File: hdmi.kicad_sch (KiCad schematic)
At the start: 10 parts, among them J6 HDMI_A, U4 AP22615AWU

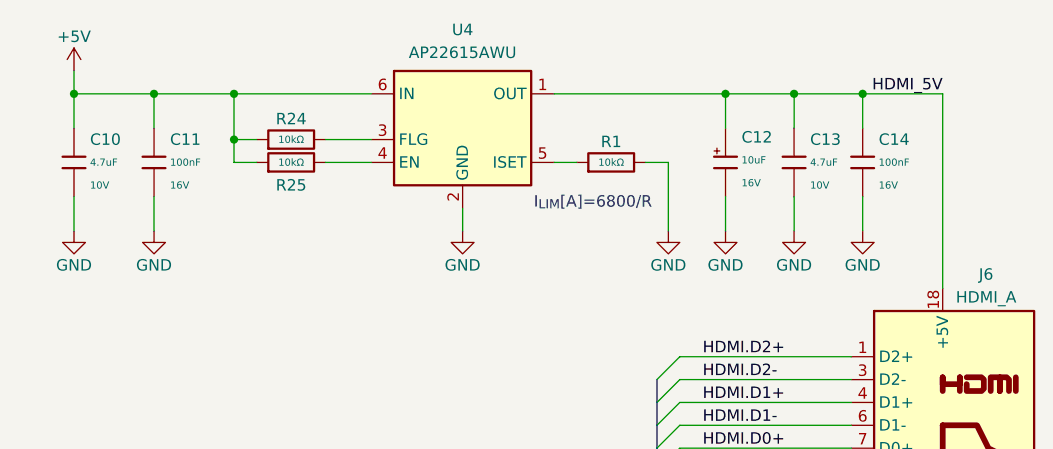
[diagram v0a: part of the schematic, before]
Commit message: [#1] WIP: Change components to ones from the global library, refactor schematic
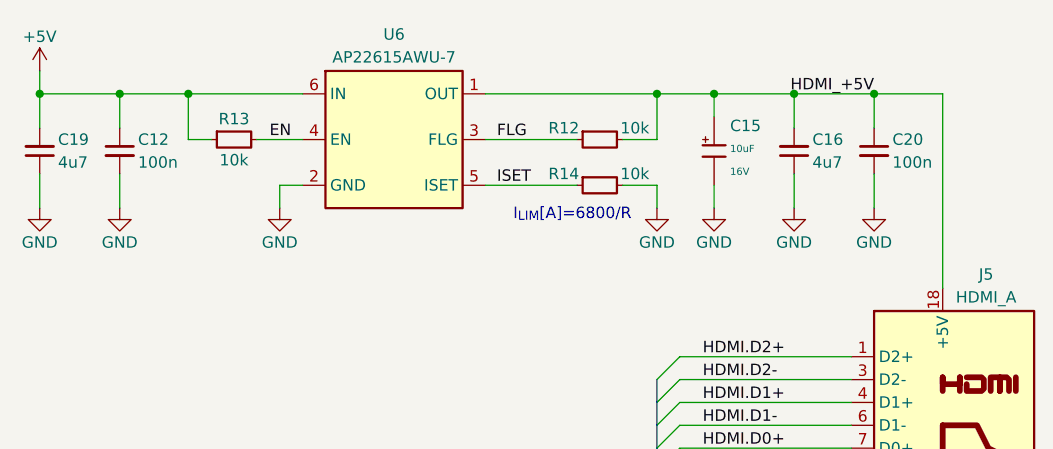
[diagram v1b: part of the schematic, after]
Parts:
- removed C10, C13: 4.7uF, PCM_JLCPCB:C_0402, symbol PCM_JLCPCB-Capacitors:0402,4.7uF
- removed C11, C14: 100nF, PCM_JLCPCB:C_0402, symbol PCM_JLCPCB-Capacitors:0402,100nF
- removed C12: 10uF, PCM_JLCPCB:C_CASE-A-3216-18(mm), symbol PCM_JLCPCB-Capacitors:CASE-A-3216-18(mm),10uF
- removed R1, R24, R25: 10kΩ, PCM_JLCPCB:R_0402, symbol PCM_JLCPCB-Resistors:0402,10kΩ
- removed U4: AP22615AWU, Package_TO_SOT_SMD:SOT-23-6, symbol Regulator_Linear:AP22615AWU
- added C12, C20: C-100n-0402, DW-footprints:C_0402_1005Metric, symbol DW-capacitors:C-100n-0402
- added C15: 10uF, PCM_JLCPCB:C_CASE-A-3216-18(mm), symbol PCM_JLCPCB-Capacitors:CASE-A-3216-18(mm),10uF
- added C16, C19: C-4u7-0402, DW-footprints:C_0402_1005Metric, symbol DW-capacitors:C-4u7-0402
- added R12, R13, R14: R-10k-0402, DW-footprints:R_0402_1005Metric, symbol DW-resistors:R-10k-0402
- added U6: AP22615AWU-7, DW-footprints:TSOT-23-6, symbol DW-ICs:AP22615AWU-7
- renumbered J6 to J5
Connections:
- net +5V: now also C12.1, C19.2, R13.1, U6.6 (IN)
- net GND: now also C12.2, C15.2, C16.1, C19.1, C20.2, R14.2, U6.2 (GND)
- net HDMI_5V renamed HDMI_+5V
- net HDMI_+5V: now also C15.1, C16.2, C20.1, R12.2, U6.1 (OUT)
- new net EN: R13.2, U6.4 (EN)
- new net FLG: R12.1, U6.3 (FLG)
- new net ISET: R14.1, U6.5 (ISET)

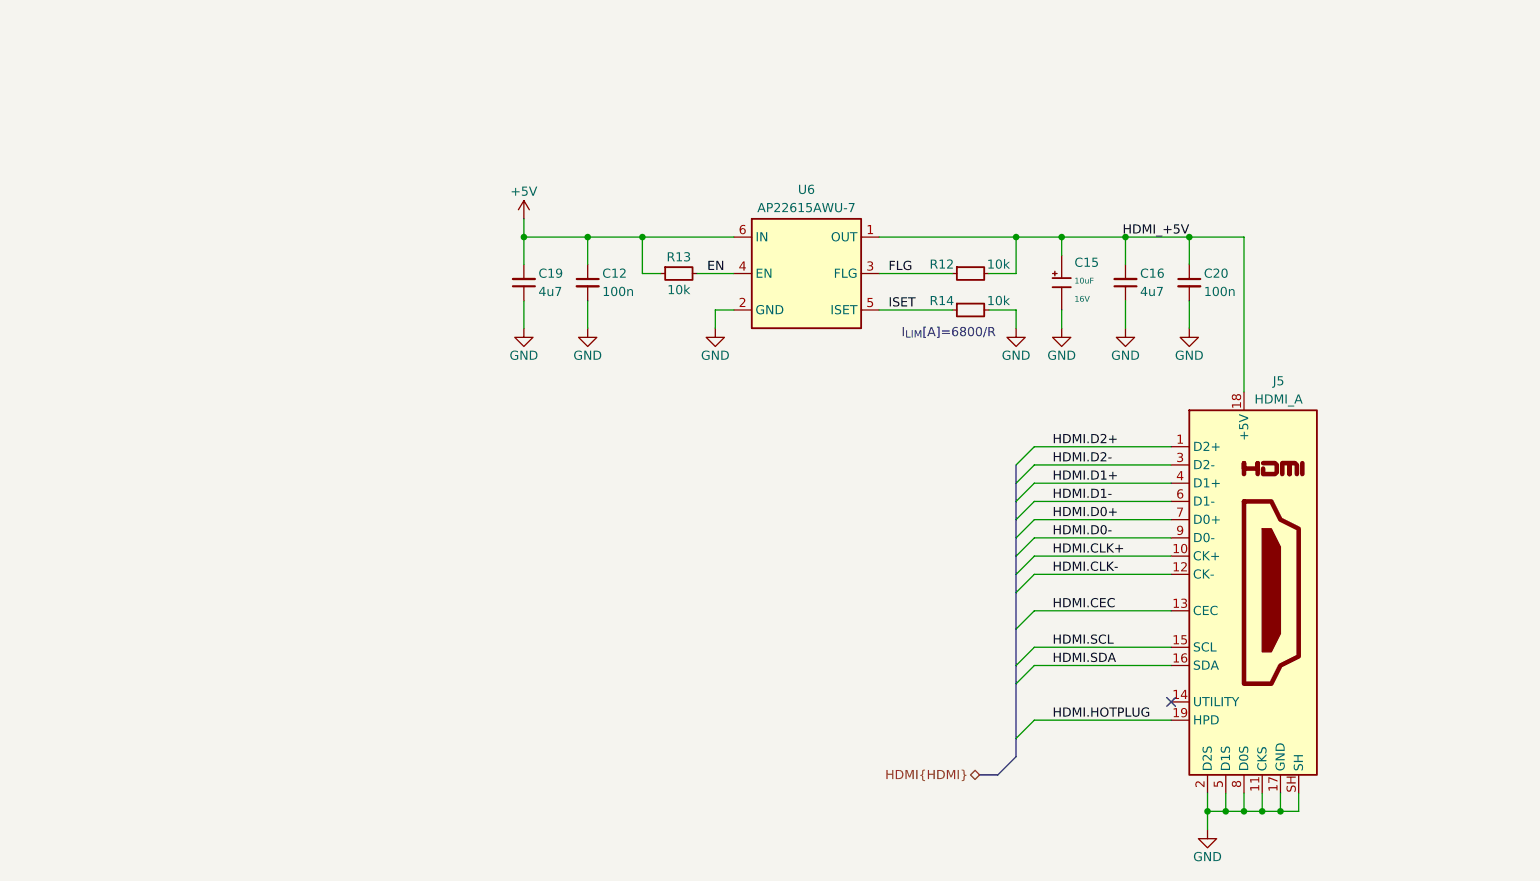
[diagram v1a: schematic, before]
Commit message: [#1] Change components to ones from the global library, add debug console, refactor schematic
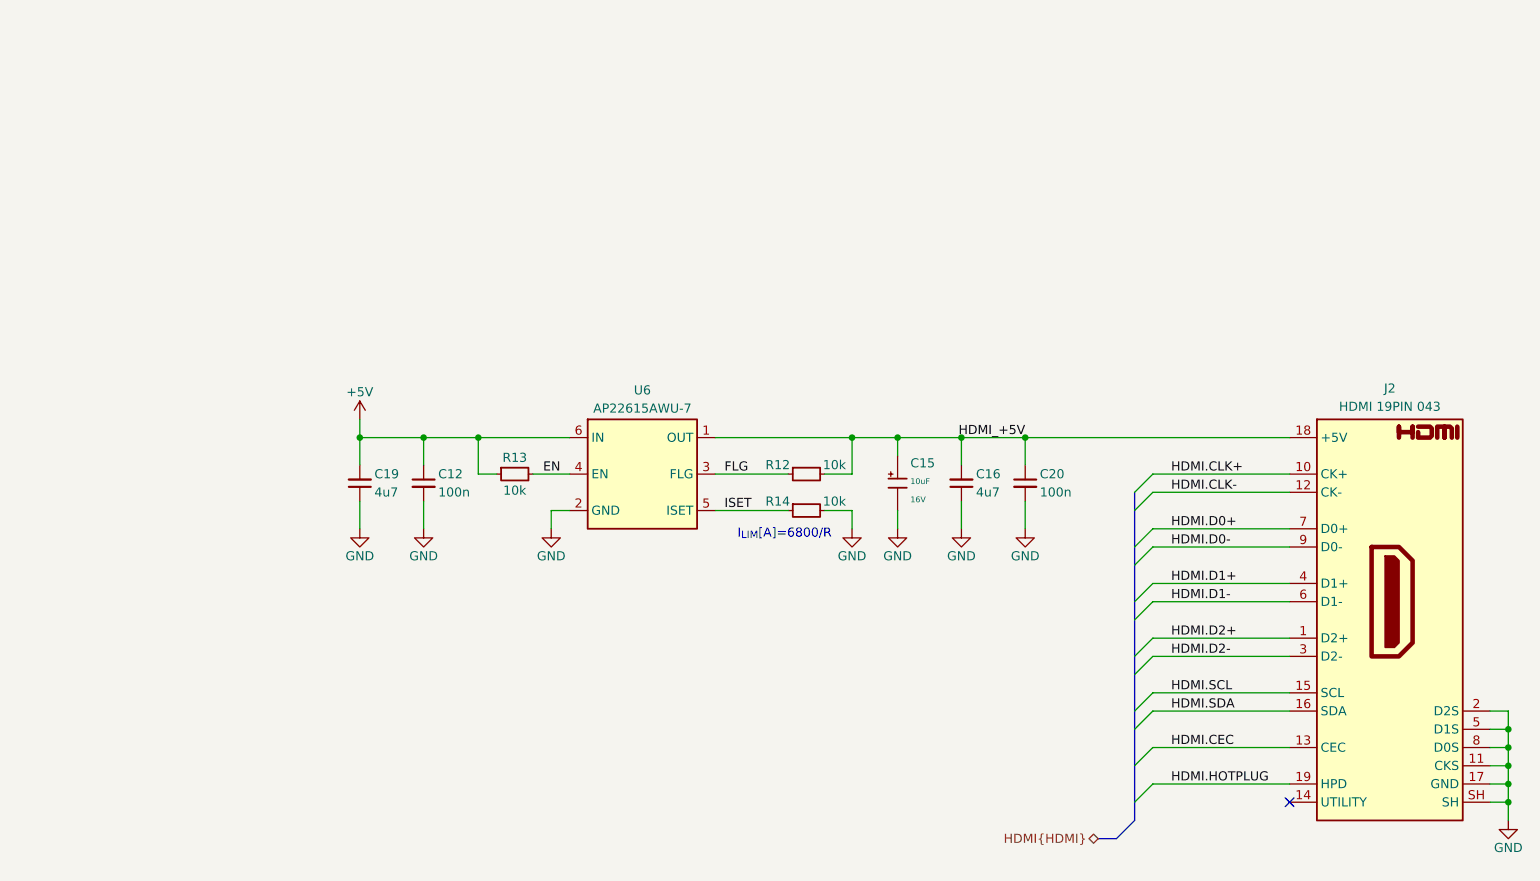
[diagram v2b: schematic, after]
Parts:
- removed J5: HDMI_A, Connector_Video:HDMI_A_Molex_208658-1001_Horizontal, symbol Connector:HDMI_A
- added J2: HDMI-A_HDMI-19PIN-043, DW-footprints:Conn_HDMI-A_HDMI-19PIN-043, symbol DW-connectors:HDMI-A_HDMI-19PIN-043
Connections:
- net GND: now also J2.11 (CKS), J2.17 (GND), J2.2 (D2S), J2.5 (D1S), J2.8 (D0S), J2.SH
- net HDMI.CEC: now also J2.13 (CEC)
- net HDMI.CLK+: now also J2.10 (CK+)
- net HDMI.CLK-: now also J2.12 (CK-)
- net HDMI.D0+: now also J2.7 (D0+)
- net HDMI.D0-: now also J2.9 (D0-)
- net HDMI.D1+: now also J2.4 (D1+)
- net HDMI.D1-: now also J2.6 (D1-)
- net HDMI.D2+: now also J2.1 (D2+)
- net HDMI.D2-: now also J2.3 (D2-)
- net HDMI.HOTPLUG: now also J2.19 (HPD)
- net HDMI.SCL: now also J2.15 (SCL)
- net HDMI.SDA: now also J2.16 (SDA)
- net HDMI_+5V: now also J2.18 (+5V)
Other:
- moved on the sheet: C12, C15, C16, C19, C20, R12, R13, R14, U6

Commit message: [#1] Re-annotate schematic
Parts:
- renumbered C15 to C10, C19 to C11, C16 to C12, C12 to C8, C20 to C9, J2 to J8, R12 to R14, R14 to R15, U6 to U2
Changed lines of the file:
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@@
 		(on_board yes)
 		(dnp no)
-		(property "Reference" "R12"
+		(property "Reference" "R14"
 			(at 172.974 134.62 0)
 			(effects
@@
 			(project "cm5-module"
 				(path "/090a8e41-87a8-4fb1-998b-60a2c0dc4cee/ad3d5826-cab5-4231-8219-c7d7eaea11f6"
-					(reference "R12")
+					(reference "R14")
 					(unit 1)
 				)
@@
 		(on_board yes)
 		(dnp no)
-		(property "Reference" "#PWR54"
+		(property "Reference" "#PWR048"
 			(at 187.96 149.86 0)
 			(effects
@@
 			(project "cm5-module"
 				(path "/090a8e41-87a8-4fb1-998b-60a2c0dc4cee/ad3d5826-cab5-4231-8219-c7d7eaea11f6"
-					(reference "#PWR54")
+					(reference "#PWR048")
 					(unit 1)
 				)
@@
 		(on_board yes)
 		(dnp no)
-		(property "Reference" "C20"
+		(property "Reference" "C9"
 			(at 207.772 135.89 90)
 			(effects
@@
 			(project "cm5-module"
 				(path "/090a8e41-87a8-4fb1-998b-60a2c0dc4cee/ad3d5826-cab5-4231-8219-c7d7eaea11f6"
-					(reference "C20")
+					(reference "C9")
 					(unit 1)
 				)
@@
 		(on_board yes)
 		(dnp no)
-		(property "Reference" "#PWR55"
+		(property "Reference" "#PWR049"
 			(at 196.85 149.86 0)
 			(effects
@@
 			(project "cm5-module"
 				(path "/090a8e41-87a8-4fb1-998b-60a2c0dc4cee/ad3d5826-cab5-4231-8219-c7d7eaea11f6"
-					(reference "#PWR55")
+					(reference "#PWR049")
 					(unit 1)
 				)
@@
 		(on_board yes)
 		(dnp no)
-		(property "Reference" "#PWR39"
+		(property "Reference" "#PWR045"
 			(at 121.92 149.86 0)
 			(effects
@@
 			(project "cm5-module"
 				(path "/090a8e41-87a8-4fb1-998b-60a2c0dc4cee/ad3d5826-cab5-4231-8219-c7d7eaea11f6"
-					(reference "#PWR39")
+					(reference "#PWR045")
 					(unit 1)
 				)
@@
 		(on_board yes)
 		(dnp no)
-		(property "Reference" "J2"
+		(property "Reference" "J8"
 			(at 256.54 123.952 0)
 			(effects
@@
 			(project ""
 				(path "/090a8e41-87a8-4fb1-998b-60a2c0dc4cee/ad3d5826-cab5-4231-8219-c7d7eaea11f6"
-					(reference "J2")
+					(reference "J8")
 					(unit 1)
 				)
@@
 		(on_board yes)
 		(dnp no)
-		(property "Reference" "C19"
+		(property "Reference" "C11"
 			(at 115.062 135.89 90)
 			(effects
@@
 			(project "cm5-module"
 				(path "/090a8e41-87a8-4fb1-998b-60a2c0dc4cee/ad3d5826-cab5-4231-8219-c7d7eaea11f6"
-					(reference "C19")
+					(reference "C11")
 					(unit 1)
 				)
@@
 		(on_board yes)
 		(dnp no)
-		(property "Reference" "#PWR56"
+		(property "Reference" "#PWR050"
 			(at 205.74 149.86 0)
 			(effects
@@
 			(project "cm5-module"
 				(path "/090a8e41-87a8-4fb1-998b-60a2c0dc4cee/ad3d5826-cab5-4231-8219-c7d7eaea11f6"
-					(reference "#PWR56")
+					(reference "#PWR050")
 					(unit 1)
 				)
@@
 		(on_board yes)
 		(dnp no)
-		(property "Reference" "#PWR40"
+		(property "Reference" "#PWR046"
 			(at 139.7 149.86 0)
 			(effects
@@
 			(project "cm5-module"
 				(path "/090a8e41-87a8-4fb1-998b-60a2c0dc4cee/ad3d5826-cab5-4231-8219-c7d7eaea11f6"
-					(reference "#PWR40")
+					(reference "#PWR046")
 					(unit 1)
 				)
@@
 		(on_board yes)
 		(dnp no)
-		(property "Reference" "C12"
+		(property "Reference" "C8"
 			(at 123.952 135.89 90)
 			(effects
@@
 			(project "cm5-module"
 				(path "/090a8e41-87a8-4fb1-998b-60a2c0dc4cee/ad3d5826-cab5-4231-8219-c7d7eaea11f6"
-					(reference "C12")
+					(reference "C8")
 					(unit 1)
 				)
@@
 		(on_board yes)
 		(dnp no)
-		(property "Reference" "U6"
+		(property "Reference" "U2"
 			(at 152.4 124.206 0)
 			(effects
@@
 			(project "cm5-module"
 				(path "/090a8e41-87a8-4fb1-998b-60a2c0dc4cee/ad3d5826-cab5-4231-8219-c7d7eaea11f6"
-					(reference "U6")
+					(reference "U2")
 					(unit 1)
 				)
@@
 		(on_board yes)
 		(dnp no)
-		(property "Reference" "#PWR35"
+		(property "Reference" "#PWR044"
 			(at 113.03 149.86 0)
 			(effects
@@
 			(project "cm5-module"
 				(path "/090a8e41-87a8-4fb1-998b-60a2c0dc4cee/ad3d5826-cab5-4231-8219-c7d7eaea11f6"
-					(reference "#PWR35")
+					(reference "#PWR044")
 					(unit 1)
 				)
@@
 		(on_board yes)
 		(dnp no)
-		(property "Reference" "C15"
+		(property "Reference" "C10"
 			(at 189.738 134.3659 0)
 			(effects
@@
 			(project "cm5-module"
 				(path "/090a8e41-87a8-4fb1-998b-60a2c0dc4cee/ad3d5826-cab5-4231-8219-c7d7eaea11f6"
-					(reference "C15")
+					(reference "C10")
 					(unit 1)
 				)
@@
 		(on_board yes)
 		(dnp no)
-		(property "Reference" "#PWR043"
+		(property "Reference" "#PWR051"
 			(at 273.05 190.5 0)
 			(effects
@@
 			(project "cm5-module"
 				(path "/090a8e41-87a8-4fb1-998b-60a2c0dc4cee/ad3d5826-cab5-4231-8219-c7d7eaea11f6"
-					(reference "#PWR043")
+					(reference "#PWR051")
 					(unit 1)
 				)
@@
 		(on_board yes)
 		(dnp no)
-		(property "Reference" "C16"
+		(property "Reference" "C12"
 			(at 198.882 135.89 90)
 			(effects
@@
 			(project "cm5-module"
 				(path "/090a8e41-87a8-4fb1-998b-60a2c0dc4cee/ad3d5826-cab5-4231-8219-c7d7eaea11f6"
-					(reference "C16")
+					(reference "C12")
 					(unit 1)
 				)
@@
 		(on_board yes)
 		(dnp no)
-		(property "Reference" "#PWR016"
+		(property "Reference" "#PWR043"
 			(at 113.03 132.08 0)
 			(effects
@@
 			(project "cm5-module"
 				(path "/090a8e41-87a8-4fb1-998b-60a2c0dc4cee/ad3d5826-cab5-4231-8219-c7d7eaea11f6"
-					(reference "#PWR016")
+					(reference "#PWR043")
 					(unit 1)
 				)
@@
 		(on_board yes)
 		(dnp no)
-		(property "Reference" "R14"
+		(property "Reference" "R15"
 			(at 172.974 139.7 0)
 			(effects
@@
 			(project "cm5-module"
 				(path "/090a8e41-87a8-4fb1-998b-60a2c0dc4cee/ad3d5826-cab5-4231-8219-c7d7eaea11f6"
-					(reference "R14")
+					(reference "R15")
 					(unit 1)
 				)
@@
 		(on_board yes)
 		(dnp no)
-		(property "Reference" "#PWR53"
+		(property "Reference" "#PWR047"
 			(at 181.61 149.86 0)
 			(effects
@@
 			(project "cm5-module"
 				(path "/090a8e41-87a8-4fb1-998b-60a2c0dc4cee/ad3d5826-cab5-4231-8219-c7d7eaea11f6"
-					(reference "#PWR53")
+					(reference "#PWR047")
 					(unit 1)
 				)

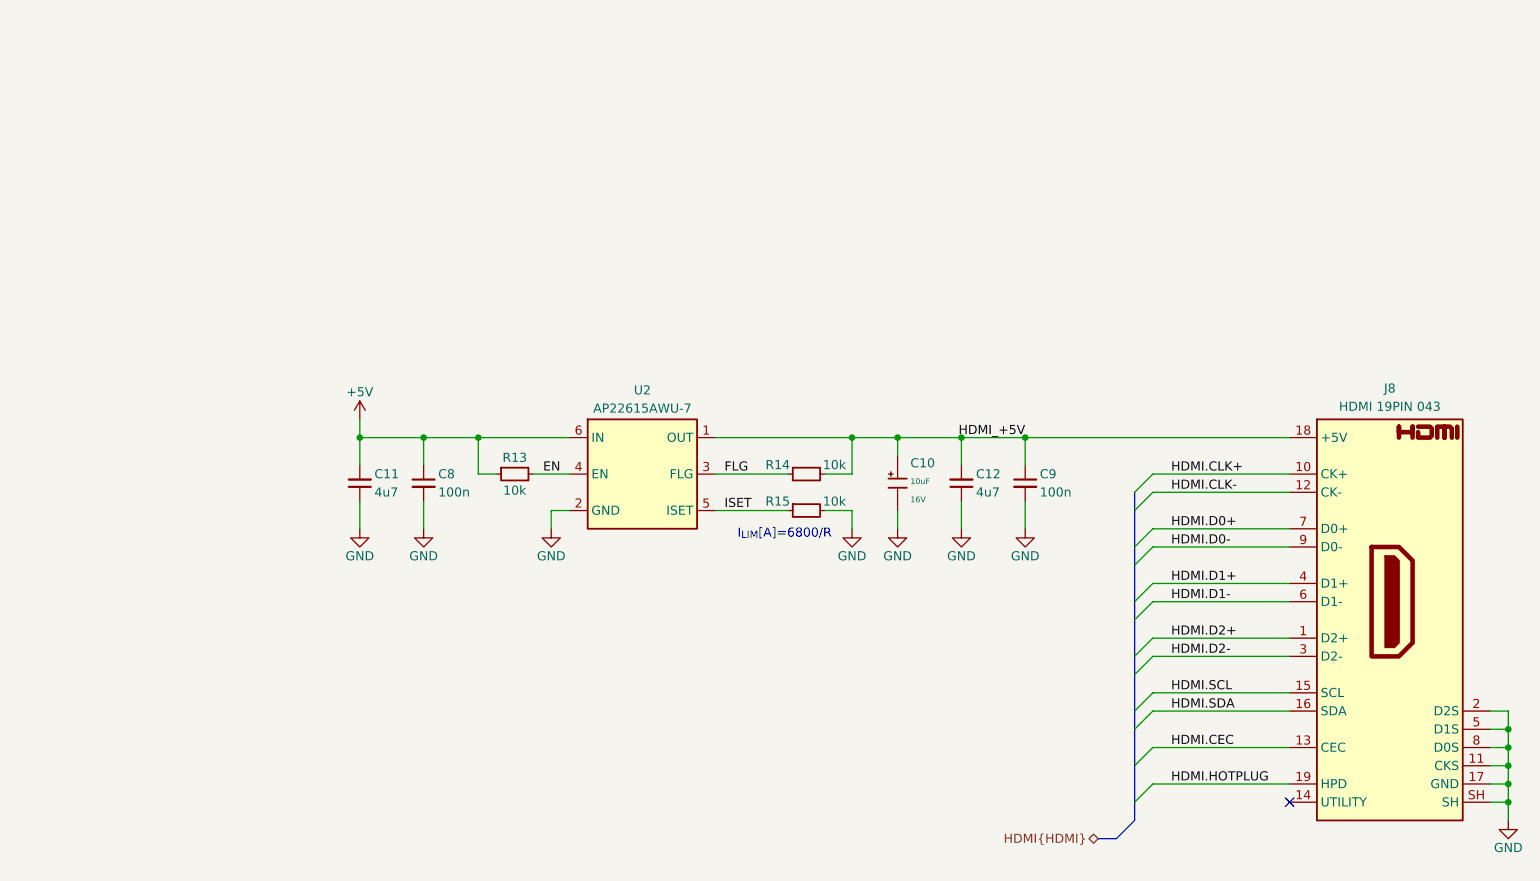
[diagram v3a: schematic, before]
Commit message: [#1] WIP: Refactor schematic
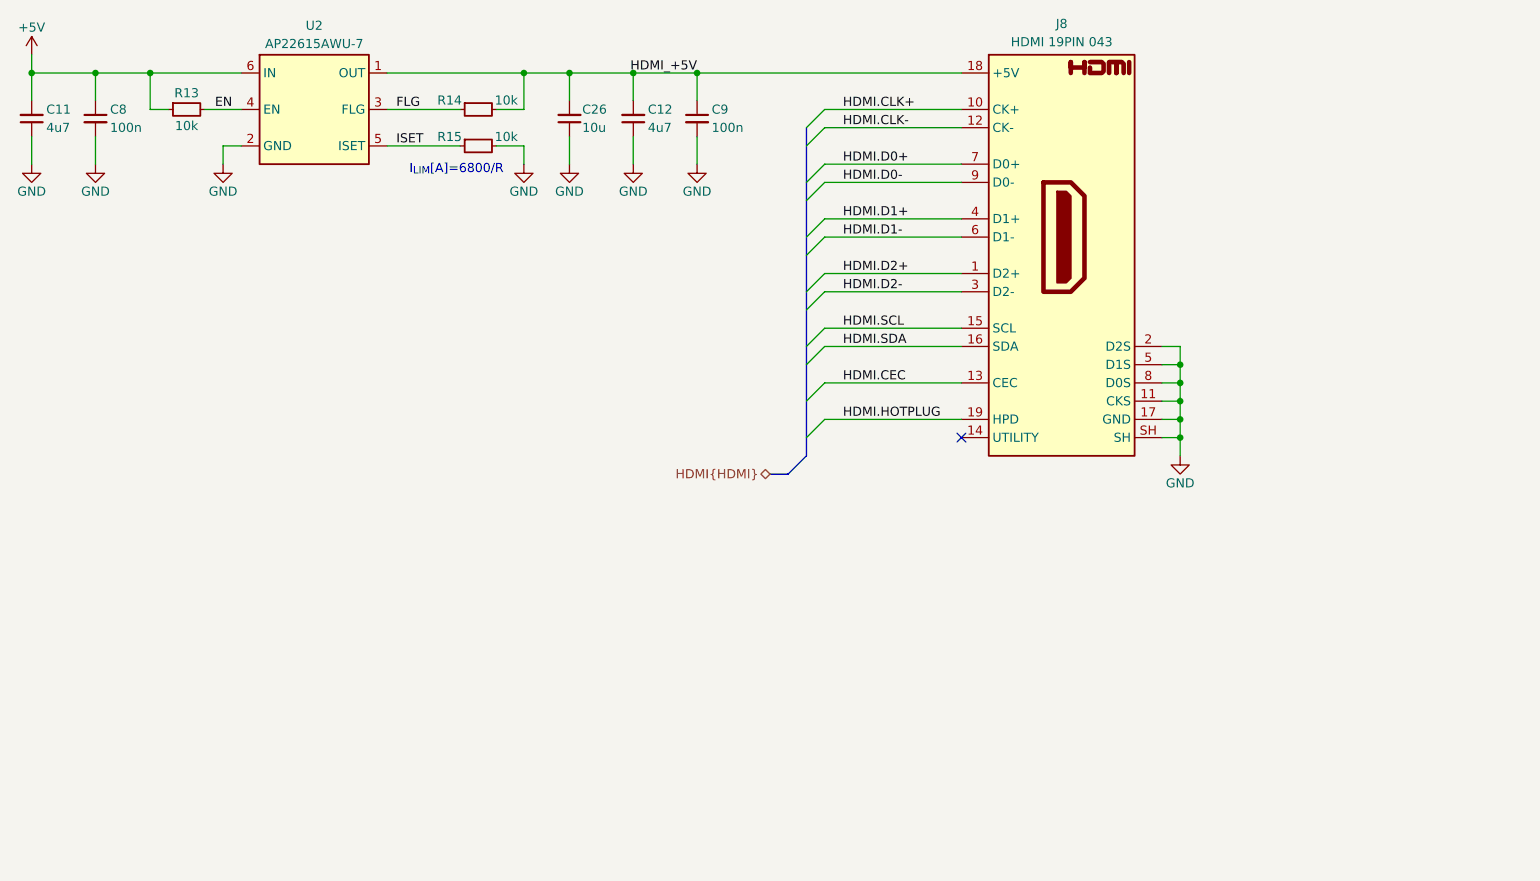
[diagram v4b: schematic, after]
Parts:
- removed C10: 10uF, PCM_JLCPCB:C_CASE-A-3216-18(mm), symbol PCM_JLCPCB-Capacitors:CASE-A-3216-18(mm),10uF
- added C26: C-10u-0603, DW-footprints:C_0603_1608Metric, symbol DW-capacitors:C-10u-0603
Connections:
- net GND: now also C26.1
- net HDMI_+5V: now also C26.2
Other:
- moved on the sheet: C11, C12, C8, C9, J8, R13, R14, R15, U2
